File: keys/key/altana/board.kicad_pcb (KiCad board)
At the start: 2 copper layers, 17.8 x 17.8 mm, 15 parts, among them J1 (+), J10 R, J11 DI, J12 DO, J2 (-), J3 C, J4 R, J5 DI, J6 DO, J7 (+)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

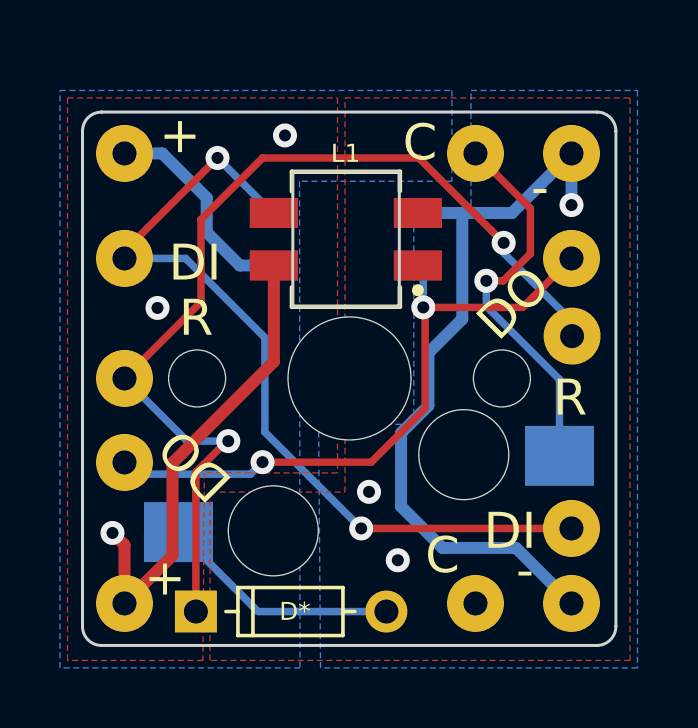
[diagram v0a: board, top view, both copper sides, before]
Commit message: Update board by using components from the project library
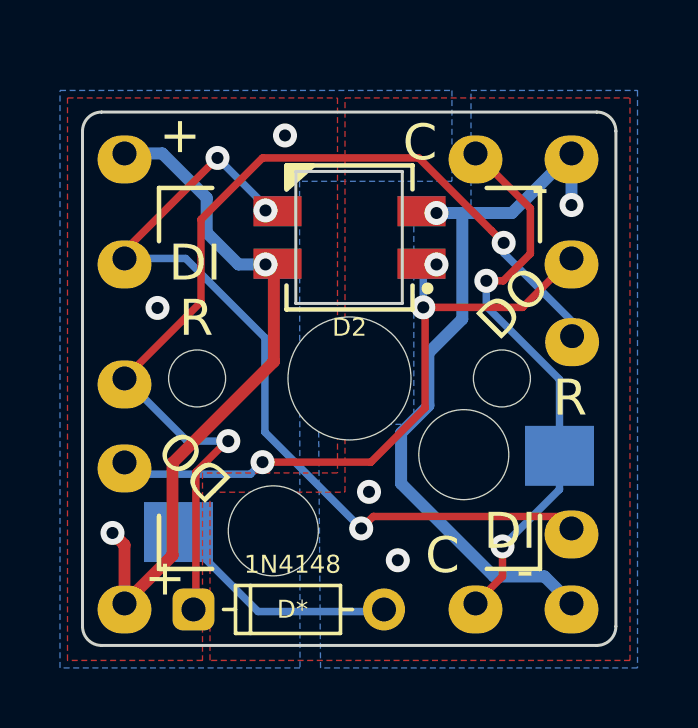
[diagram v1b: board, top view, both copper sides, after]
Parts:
- removed L1: SK6812MINI, kbd:SK6812MINI_rev
- added D2: SK6812MINI, Altana:SK6812MINI, F.Cu at (158.3, 123.8)
- D1: value D -> 1N4148; footprint footprint:diode -> Altana:diode
- J1, J10, J11, J12, J2, J3, J4, J5, J6, J7, J8, J9: footprint kbd:wirepad-h0.8mm-d1.8mm -> Altana:wirepad
- SW1: footprint kbd:MX_Hotswap_single -> Altana:Switch_MX_Hotswap
- moved D1 0.11 mm to (153.1, 136.2)
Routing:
- net /key/COL_N: track 12.8 -> 18.9 mm, vias 1 -> 3
- net GND: track 25.2 -> 24.7 mm, vias 3 -> 4
- net /key/LED_DI: track 27.7 -> 28.1 mm, vias 2 -> 3
- net /key/LED_DO: track 21.3 -> 21.2 mm, vias 2 -> 3
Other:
- outline, holes or cut-outs redrawn

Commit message: Add extra capacitor and make it more flexible for panels
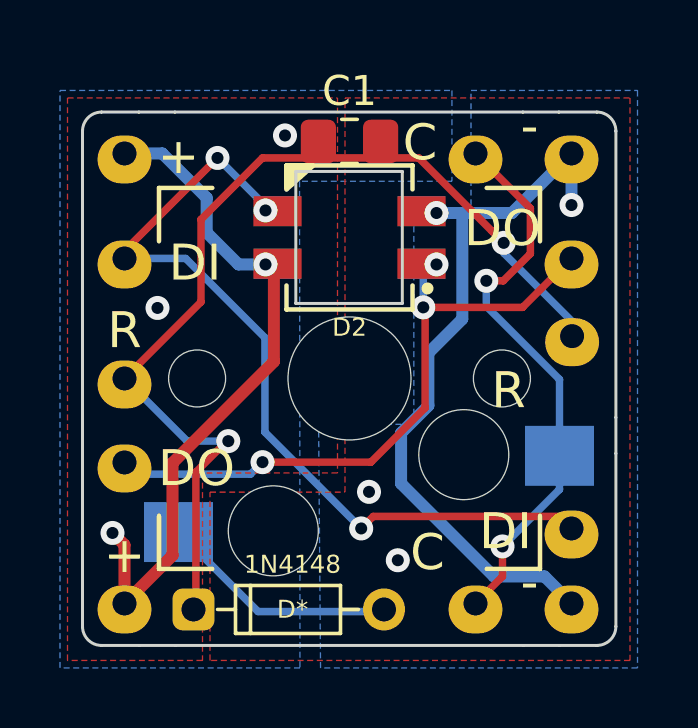
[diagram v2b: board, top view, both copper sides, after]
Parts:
- added C1: C_Small, Capacitor_SMD:C_0805_2012Metric_Pad1.18x1.45mm_HandSolder, F.Cu at (158.3, 120.6)
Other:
- outline, holes or cut-outs redrawn
- board text added: "Connect GND and COL[N+1] Here"
- board text added: "Connect GND and COL[N-1] Here"
- board text added: "Connect ROW[N+1] Here"
- board text added: "Connect ROW[N-1] Here"
- board text added: "Connect VCC Here"
- board text added: "Connected panels can be created by removing the edge on the conrners that have this bridge path"
